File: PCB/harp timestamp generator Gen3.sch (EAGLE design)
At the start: 140 parts, among them IC1 MCP73831T-2ATI/OT, IC10 SN74LVC1G125DBVT, IC11 TLV70033DDCR, IC12 SI8621BC-B-IS, IC13 SI8621BC-B-IS, IC14 SI8621BC-B-IS, IC15 SI8621BC-B-IS, IC16 SI8621BC-B-IS, IC17 SI8621BC-B-IS, IC18 SN74LVC1G125DBVT, IC19 SN74LVC1G125DBVT, IC2 USBLC6-2SC6, IC3 FT232RL, IC4 ICL7673CBAZA-T, IC5 TLV70033DDCR, IC6 ATXMEGA16A4U-AU, IC7 M74VHC1GT126DF1G, IC8 M74VHC1GT126DF1G, IC9 M74VHC1GT126DF1G, Q1 RTU002P02T106, Q2 BC817-40W, Q3 BC817-40LT1SMD, Q4 DMG1012UW, Q5 DMP2035U-7, T1 BC850, T10 BC850, T2 BC850, T3 BC850, T4 BC850, T5 BC850, T6 BC850, T7 BC850, T8 BC850, T9 BC850, X1 B2B-PH-K-S(LF)(SN)

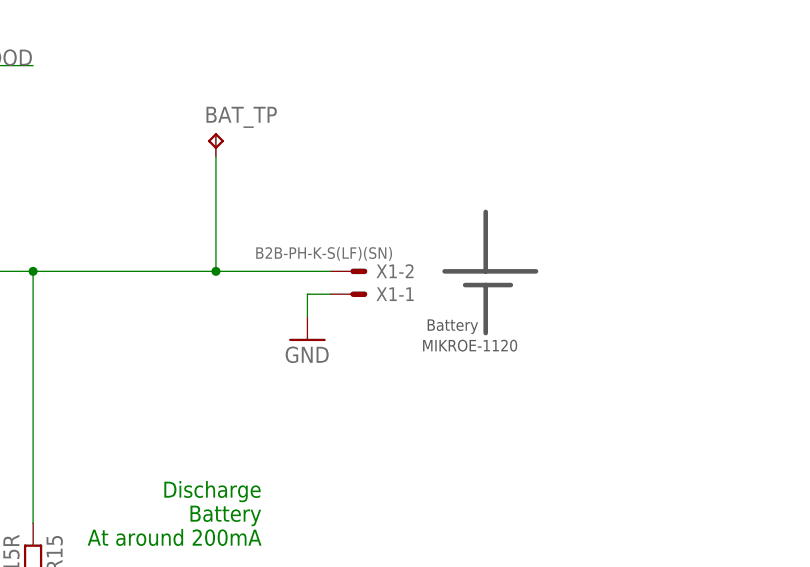
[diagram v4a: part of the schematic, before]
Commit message: Corrected X1 PN and PCB's orientation.
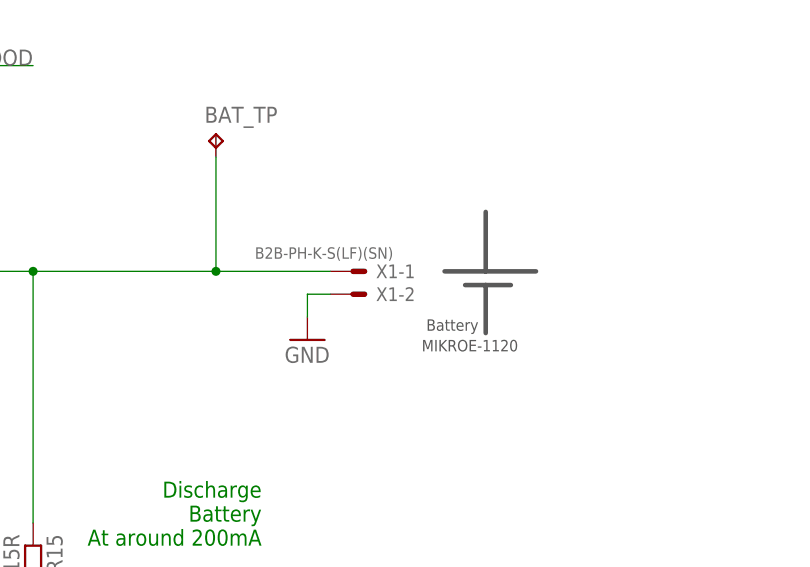
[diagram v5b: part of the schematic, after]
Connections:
- net GND: now also X1-2.S; no longer X1-1.S
- net V_BATT: now also X1-1.S; no longer X1-2.S
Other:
- moved on the sheet: X1-1, X1-2
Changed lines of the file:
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@@
 <?xml version="1.0" encoding="utf-8"?>
 <!DOCTYPE eagle SYSTEM "eagle.dtd">
-<eagle version="9.6.2">
+<eagle version="9.5.1">
 <drawing>
 <settings>
@@
 <attribute name="DIGKEYPN" x="500.38" y="373.38" size="1.778" layer="96" rot="MR0" display="off"/>
 </instance>
-<instance part="X1" gate="-2" x="340.36" y="447.04" smashed="yes">
-<attribute name="NAME" x="342.9" y="446.278" size="1.524" layer="95"/>
-<attribute name="MPN" x="340.36" y="447.04" size="1.778" layer="96" display="off"/>
-<attribute name="DIGKEYPN" x="340.36" y="447.04" size="1.778" layer="96" display="off"/>
-<attribute name="MPN" x="340.36" y="447.04" size="1.778" layer="96" display="off"/>
-<attribute name="DIGKEYPN" x="340.36" y="447.04" size="1.778" layer="96" display="off"/>
-</instance>
-<instance part="X1" gate="-1" x="340.36" y="444.5" smashed="yes">
+<instance part="X1" gate="-2" x="340.36" y="444.5" smashed="yes">
 <attribute name="NAME" x="342.9" y="443.738" size="1.524" layer="95"/>
-<attribute name="VALUE" x="329.438" y="448.437" size="1.27" layer="96"/>
 <attribute name="MPN" x="340.36" y="444.5" size="1.778" layer="96" display="off"/>
 <attribute name="DIGKEYPN" x="340.36" y="444.5" size="1.778" layer="96" display="off"/>
@@
 <attribute name="DIGKEYPN" x="340.36" y="444.5" size="1.778" layer="96" display="off"/>
 </instance>
+<instance part="X1" gate="-1" x="340.36" y="447.04" smashed="yes">
+<attribute name="NAME" x="342.9" y="446.278" size="1.524" layer="95"/>
+<attribute name="VALUE" x="329.438" y="448.437" size="1.27" layer="96"/>
+<attribute name="MPN" x="340.36" y="447.04" size="1.778" layer="96" display="off"/>
+<attribute name="DIGKEYPN" x="340.36" y="447.04" size="1.778" layer="96" display="off"/>
+<attribute name="MPN" x="340.36" y="447.04" size="1.778" layer="96" display="off"/>
+<attribute name="DIGKEYPN" x="340.36" y="447.04" size="1.778" layer="96" display="off"/>
+</instance>
 <instance part="GND54" gate="1" x="335.28" y="439.42" smashed="yes">
 <attribute name="VALUE" x="332.74" y="436.88" size="1.778" layer="96"/>
@@
 </segment>
 <segment>
-<pinref part="X1" gate="-1" pin="S"/>
-<wire x1="337.82" y1="444.5" x2="335.28" y2="444.5" width="0.1524" layer="91"/>
 <pinref part="GND54" gate="1" pin="GND"/>
 <wire x1="335.28" y1="444.5" x2="335.28" y2="441.96" width="0.1524" layer="91"/>
+<pinref part="X1" gate="-2" pin="S"/>
+<wire x1="337.82" y1="444.5" x2="335.28" y2="444.5" width="0.1524" layer="91"/>
 </segment>
 <segment>
@@
 <net name="V_BATT" class="0">
 <segment>
-<pinref part="X1" gate="-2" pin="S"/>
 <wire x1="200.66" y1="459.74" x2="231.14" y2="459.74" width="0.1524" layer="91"/>
 <wire x1="231.14" y1="459.74" x2="231.14" y2="472.44" width="0.1524" layer="91"/>
@@
 <junction x="325.12" y="447.04"/>
 <label x="236.22" y="447.04" size="2.54" layer="95"/>
+<pinref part="X1" gate="-1" pin="S"/>
 </segment>
 </net>
